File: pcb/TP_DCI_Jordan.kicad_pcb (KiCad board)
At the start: 2 copper layers, 0 parts

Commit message: huella SMD para PCF8574 y DIPSwitch
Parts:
- added C1: 220uF/16V, miCapacitor_THT:Electrolitico_10uF, F.Cu at (150.8, 93.5)
- added C2: 100uF/16V, miCapacitor_THT:Electrolitico_10uF, F.Cu at (131.9, 101.9)
- added C3: 0.1uF/16V, miCapacitor_THT:Lenteja_Ceramica, F.Cu at (131.7, 107.0)
- added C4: 0.1uF/16V, miCapacitor_THT:Lenteja_Ceramica, F.Cu at (138.5, 104.1)
- added C5: 10nF/16V, miCapacitor_THT:Lenteja_Ceramica, F.Cu at (138.5, 100.4)
- added D1: LED, LED_THT:LED_D3.0mm_Clear, F.Cu at (131.2, 111.6)
- added D2: 5v, miDiodo:miZener, F.Cu at (135.4, 82.0)
- added J1: MICRO, Connector_Phoenix_MSTB:PhoenixContact_MSTBVA_2,5_4-G_1x04_P5.00mm_Vertical, F.Cu at (103.8, 76.6)
- added J2: Display, Connector_PinHeader_2.54mm:PinHeader_1x18_P2.54mm_Vertical, F.Cu at (170.7, 38.7)
- added L1: 47uH, Inductor_THT:L_Axial_L5.3mm_D2.2mm_P7.62mm_Horizontal_Vishay_IM-1, F.Cu at (142.1, 84.3)
- added R1: 100, Resistor_THT:R_Axial_DIN0207_L6.3mm_D2.5mm_P7.62mm_Horizontal, F.Cu at (142.1, 80.4)
- added R2: 100, Resistor_THT:R_Axial_DIN0207_L6.3mm_D2.5mm_P7.62mm_Horizontal, F.Cu at (152.8, 82.8)
- added R3: 2k2, Resistor_THT:R_Axial_DIN0207_L6.3mm_D2.5mm_P7.62mm_Horizontal, F.Cu at (152.8, 86.9)
- added R4: 10k, Resistor_THT:R_Axial_DIN0207_L6.3mm_D2.5mm_P7.62mm_Horizontal, F.Cu at (131.1, 88.2)
- added R5: 10k, Resistor_THT:R_Axial_DIN0207_L6.3mm_D2.5mm_P7.62mm_Horizontal, F.Cu at (141.9, 88.2)
- added R6: 10k, Resistor_THT:R_Axial_DIN0207_L6.3mm_D2.5mm_P7.62mm_Horizontal, F.Cu at (131.1, 92.2)
- added RV1: 10k, miPotenciometro_RV09:miPote10k_3362P, F.Cu at (144.4, 94.5)
- added SW1: SW_DIP_x03, miConector:DIPSwitch_03, F.Cu at (162.3, 53.6)
- added U1: PCF8574, miSMD:SOIC127P1030X265-16N, F.Cu at (149.2, 49.2)
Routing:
- net /RS: track 0.00 -> 17.9 mm
- net /R-W: track 0.00 -> 14.9 mm
- net /D7: track 0.00 -> 13.7 mm
- net /D6: track 0.00 -> 11.4 mm
- net /EN: track 0.00 -> 11.0 mm
- net /D5: track 0.00 -> 8.70 mm
- net /D4: track 0.00 -> 6.39 mm
- net Net-(R6-Pad1): track 0.00 -> 5.12 mm
- net Net-(R5-Pad1): track 0.00 -> 4.59 mm
- net Net-(R4-Pad1): track 0.00 -> 4.10 mm

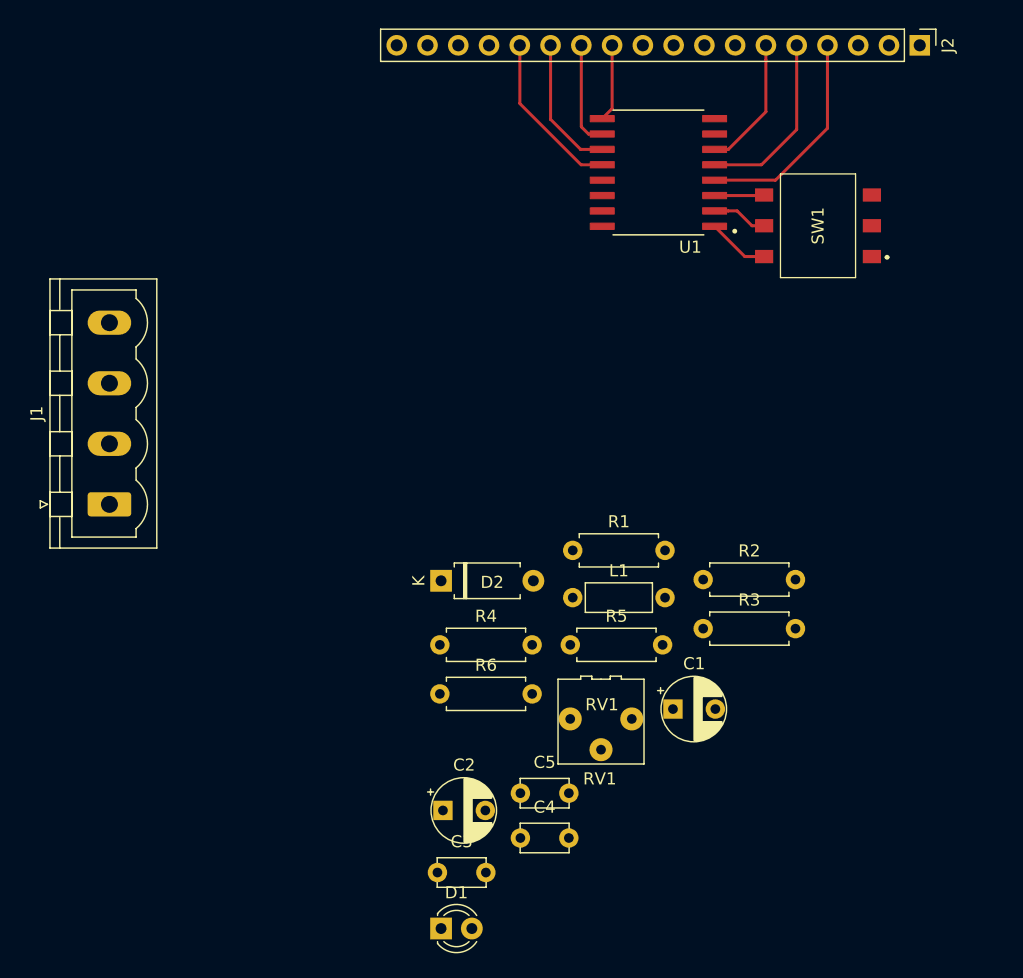
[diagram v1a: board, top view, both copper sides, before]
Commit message: creación de PCB y orden de primeros elementos
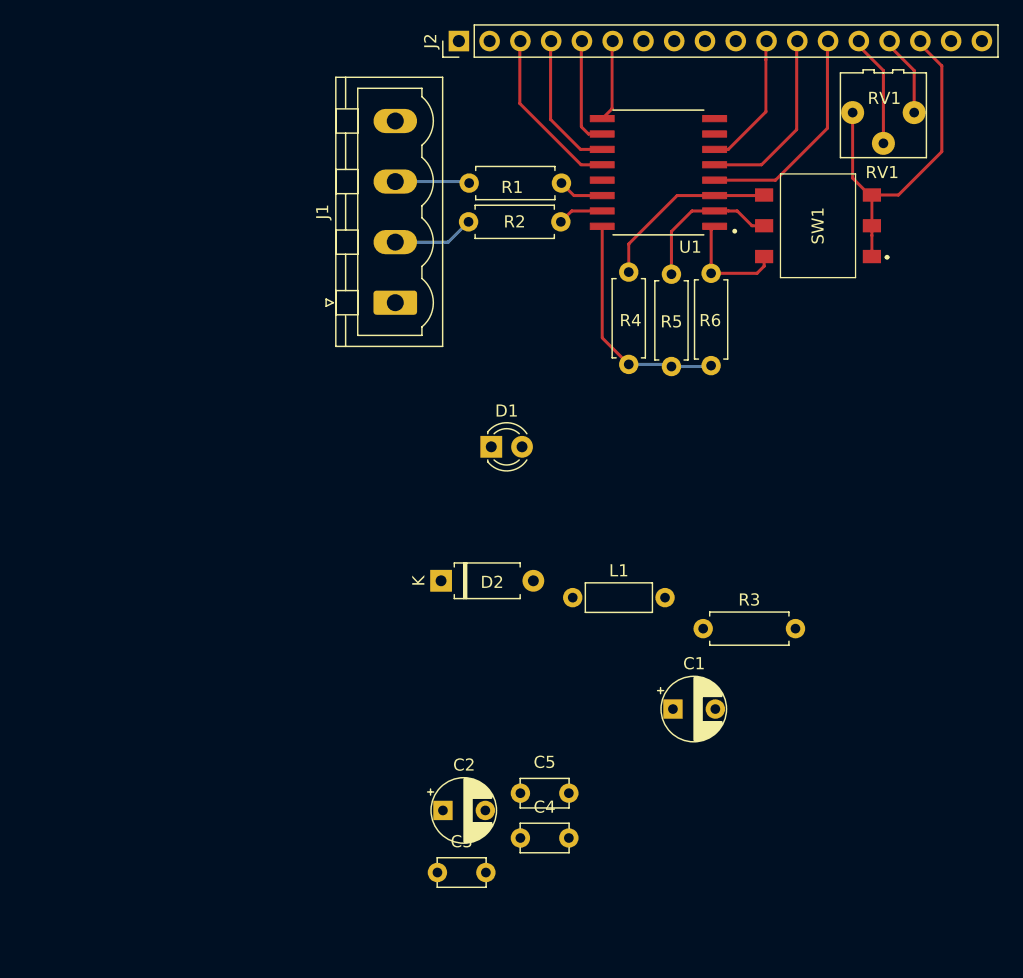
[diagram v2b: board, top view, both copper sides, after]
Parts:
- J2: footprint Connector_PinHeader_2.54mm:PinHeader_1x18_P2.54mm_Vertical -> miConector:LCD_16x2_dosTipos
- moved RV1 55.2 mm to (167.7, 44.5)
- moved R6 41.3 mm to (153.5, 57.5), turned to 270 degrees
- moved D1 40.0 mm to (135.3, 71.8)
- moved J2 38.1 mm to (132.7, 38.4), turned to 90 degrees
- moved R2 35.3 mm to (133.5, 53.3)
- moved R4 34.5 mm to (146.7, 57.4), turned to 270 degrees
- moved R5 31.7 mm to (150.2, 57.6), turned to 270 degrees
- moved R1 31.5 mm to (133.5, 50.1)
- moved J1 28.9 mm to (127.4, 60.0)
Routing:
- net GND: track 0.00 -> 29.5 mm
- net VDD: track 0.00 -> 25.6 mm
- net Net-(R4-Pad1): track 4.10 -> 15.2 mm
- net /V0: track 0.00 -> 8.96 mm
- net Net-(R5-Pad1): track 4.59 -> 12.4 mm
- net /SDA: track 0.00 -> 6.74 mm
- net /SCL: track 0.00 -> 6.15 mm
- net Net-(R6-Pad1): track 5.12 -> 9.42 mm
- net Net-(R1-Pad2): track 0.00 -> 3.79 mm
- net Net-(R2-Pad2): track 0.00 -> 3.79 mm

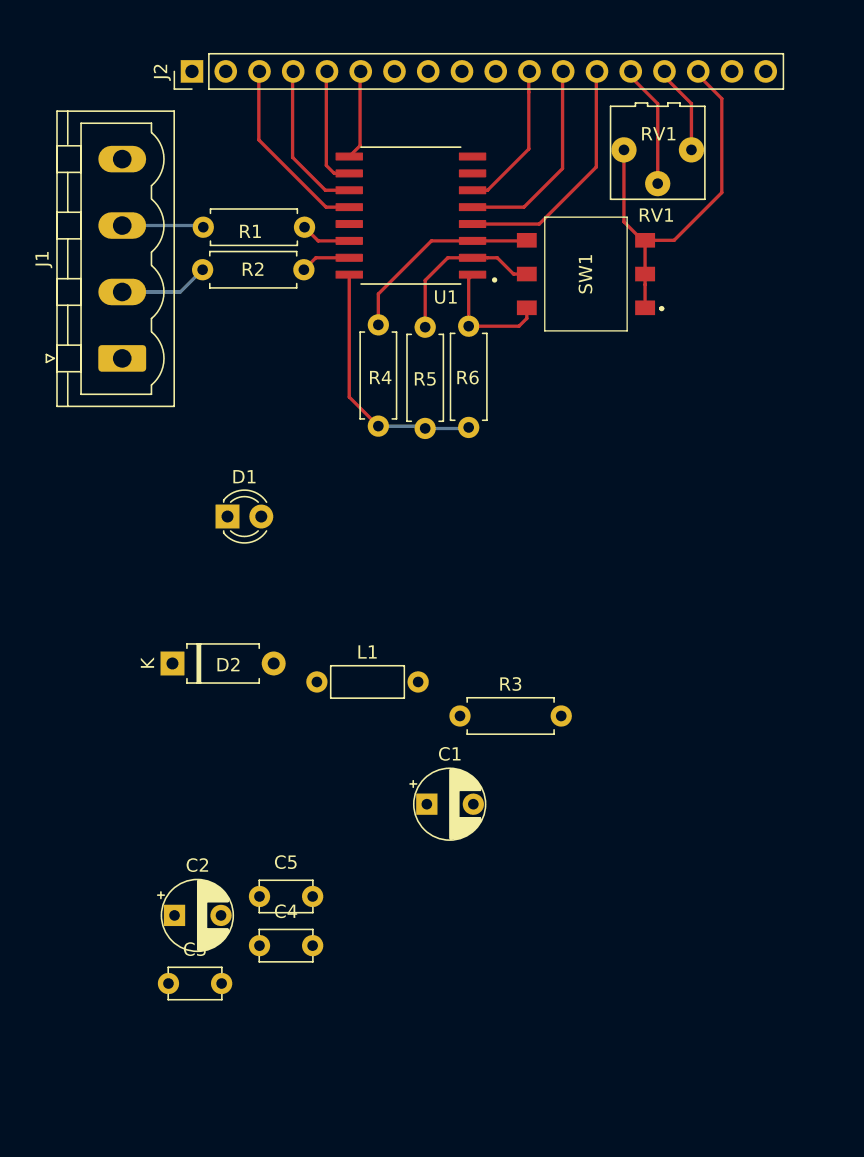
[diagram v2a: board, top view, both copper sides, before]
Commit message: Se agrega borde y margen de PCB
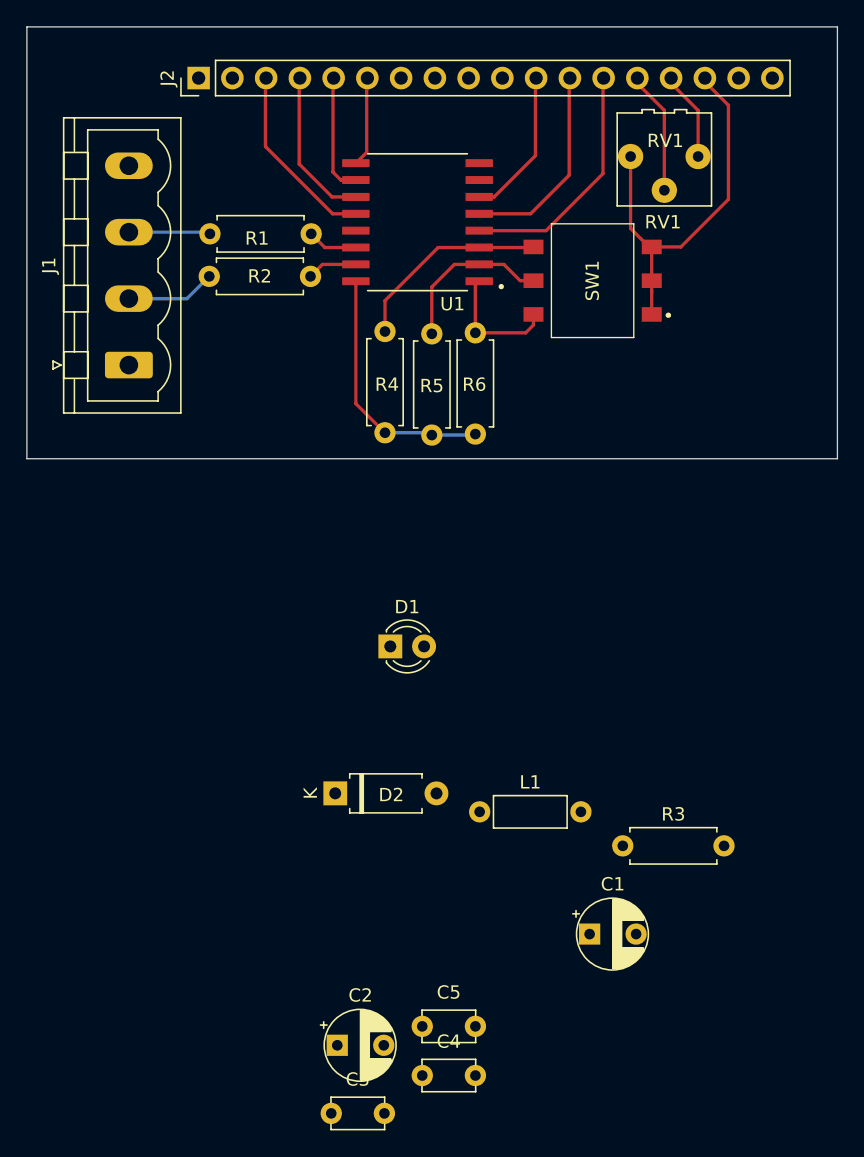
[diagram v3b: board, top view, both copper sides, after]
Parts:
- moved C1 15.7 mm to (163.1, 103.3)
- moved C4 15.7 mm to (150.8, 113.9)
- moved C5 15.7 mm to (150.8, 110.2)
- moved D1 15.7 mm to (147.6, 81.6)
- moved L1 15.7 mm to (154.3, 94.1)
- moved R3 15.7 mm to (165.1, 96.6)
- moved C2 15.7 mm to (144.1, 111.6)
- moved C3 15.7 mm to (143.9, 116.8)
- moved D2 15.7 mm to (147.7, 91.7)
- moved J1 0.71 mm to (127.9, 60.5)
- moved J2 0.71 mm to (133.2, 38.9)
- moved R1 0.71 mm to (134.0, 50.6)
- moved R2 0.71 mm to (134.0, 53.8)
- moved R4 0.71 mm to (147.2, 57.9)
- moved R5 0.71 mm to (150.7, 58.1)
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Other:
- board outline added: 61 x 32.5 mm

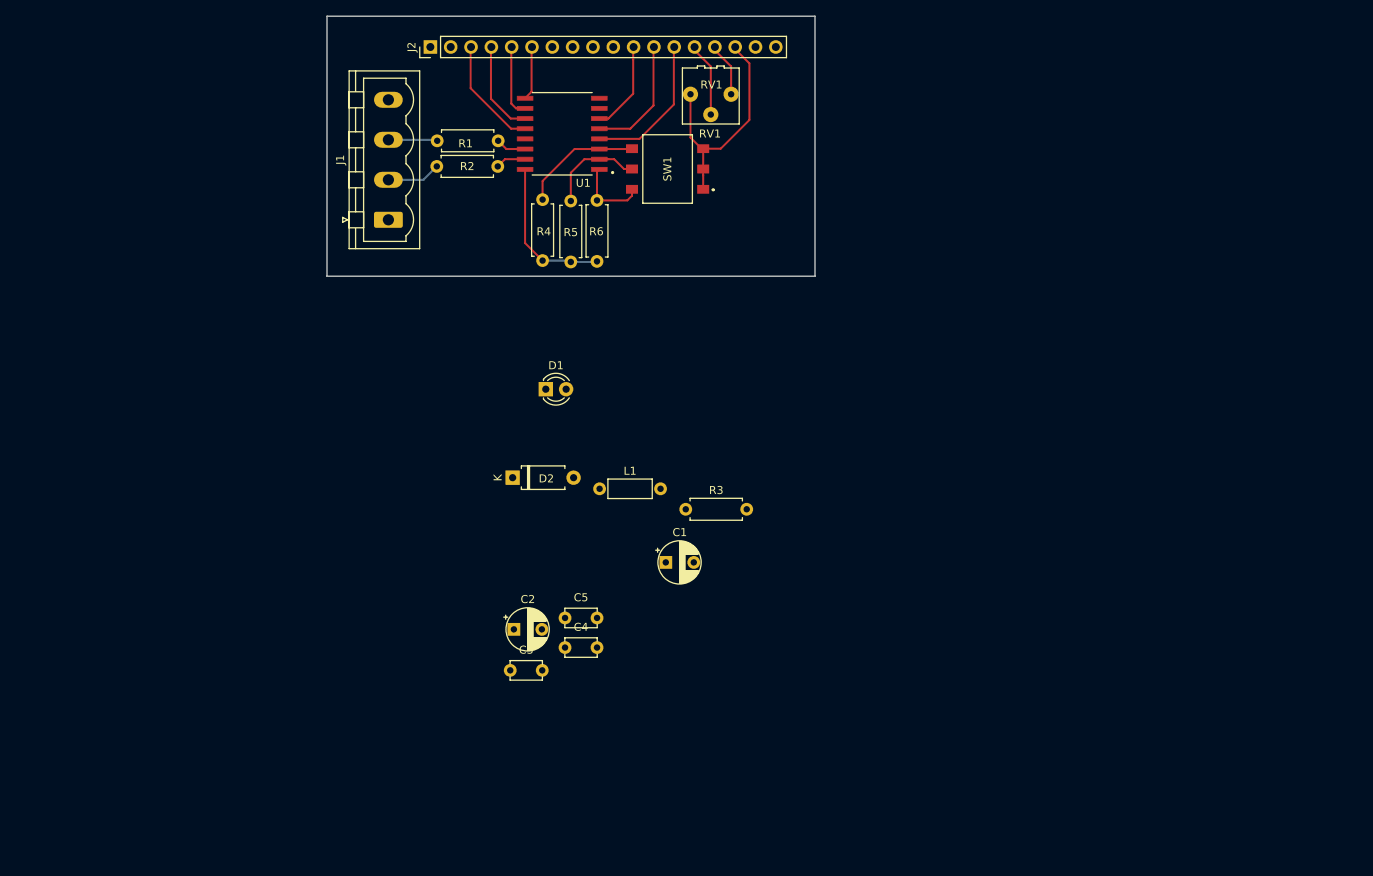
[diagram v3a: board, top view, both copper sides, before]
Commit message: actualización de PCB con primeras huellas SMD
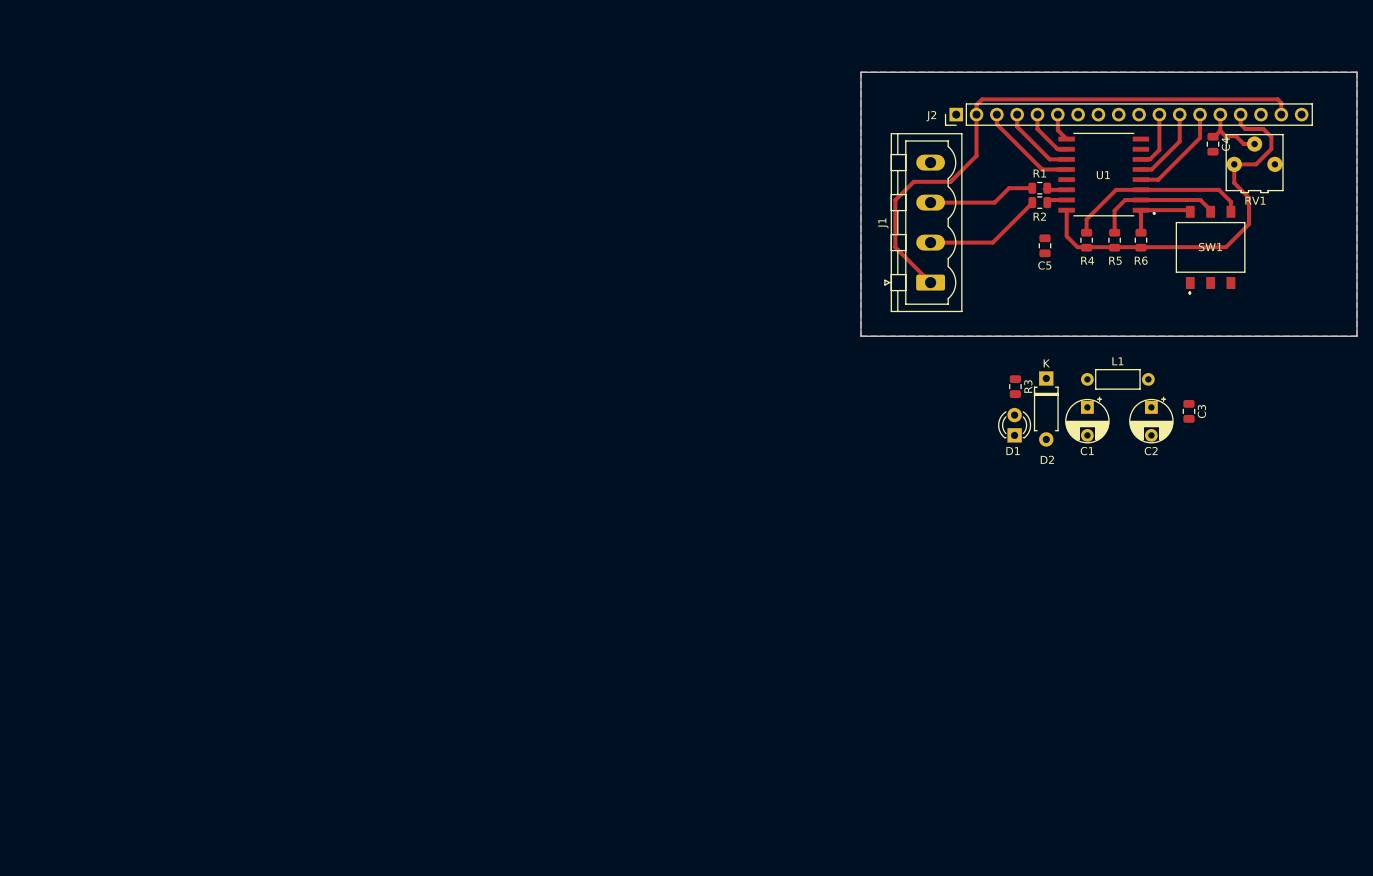
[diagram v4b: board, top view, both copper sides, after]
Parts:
- C3, C4, C5: footprint miCapacitor_THT:Lenteja_Ceramica -> Capacitor_SMD:C_0805_2012Metric
- D2: value 5v -> 5v1
- R1, R2, R3, R4, R5, R6: footprint Resistor_THT:R_Axial_DIN0207_L6.3mm_D2.5mm_P7.62mm_Horizontal -> Resistor_SMD:R_0805_2012Metric
- moved C4 102.0 mm to (231.0, 51.0), turned to 270 degrees
- moved C3 90.1 mm to (228.0, 84.4), turned to 270 degrees
- moved C2 83.7 mm to (223.3, 84.4), turned to 270 degrees
- moved R1 75.6 mm to (209.3, 56.5)
- moved R2 75.5 mm to (209.3, 58.3)
- moved C5 75.3 mm to (210.0, 63.7), turned to 270 degrees
- moved SW1 68.6 mm to (230.7, 63.9), turned to 0 degrees
- moved RV1 68.5 mm to (236.2, 53.3), turned to 180 degrees
- moved J1 68.2 mm to (195.7, 68.3)
- moved R4 68.2 mm to (215.2, 63.0)
- moved R6 68.2 mm to (222.0, 63.0)
- moved R5 68.2 mm to (218.7, 63.0)
- moved U1 67.9 mm to (217.3, 54.8)
- moved J2 66.3 mm to (198.9, 47.3)
- moved D2 63.8 mm to (211.1, 84.5), turned to 270 degrees
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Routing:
- net /Vin: track 0.00 -> 71.0 mm
- net GND: track 29.5 -> 0.00 mm
- net VDD: track 25.6 -> 48.7 mm
- net /SDA: track 6.74 -> 14.8 mm
- net Net-(R4-Pad1): track 15.2 -> 23.2 mm
- net /SCL: track 6.15 -> 13.5 mm
- net /RS: track 17.9 -> 12.5 mm
- net /R-W: track 14.9 -> 9.66 mm
- net /EN: track 11.0 -> 7.21 mm
- net Net-(R5-Pad1): track 12.4 -> 16.1 mm
- net /D4: track 6.39 -> 3.51 mm
- net /D5: track 8.70 -> 6.50 mm
- net /D6: track 11.4 -> 9.40 mm
- net /D7: track 13.7 -> 12.3 mm
- net Net-(R2-Pad2): track 3.79 -> 2.87 mm
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- added copper zone on B.Cu, net GND
- added copper zone on F.Cu, net GND
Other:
- board size 61 x 32.5 mm -> 62 x 33 mm
- net class Default: clearance 0.2 -> 0.4; trace_width 0.25 -> 0.5
- rule trace_clearance: 0.2 -> 0.4
